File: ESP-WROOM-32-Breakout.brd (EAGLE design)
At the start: 34.5 x 40 mm, 10 parts, among them SW1 PROG, SW2 RST, U3 ESP-WROOM-32

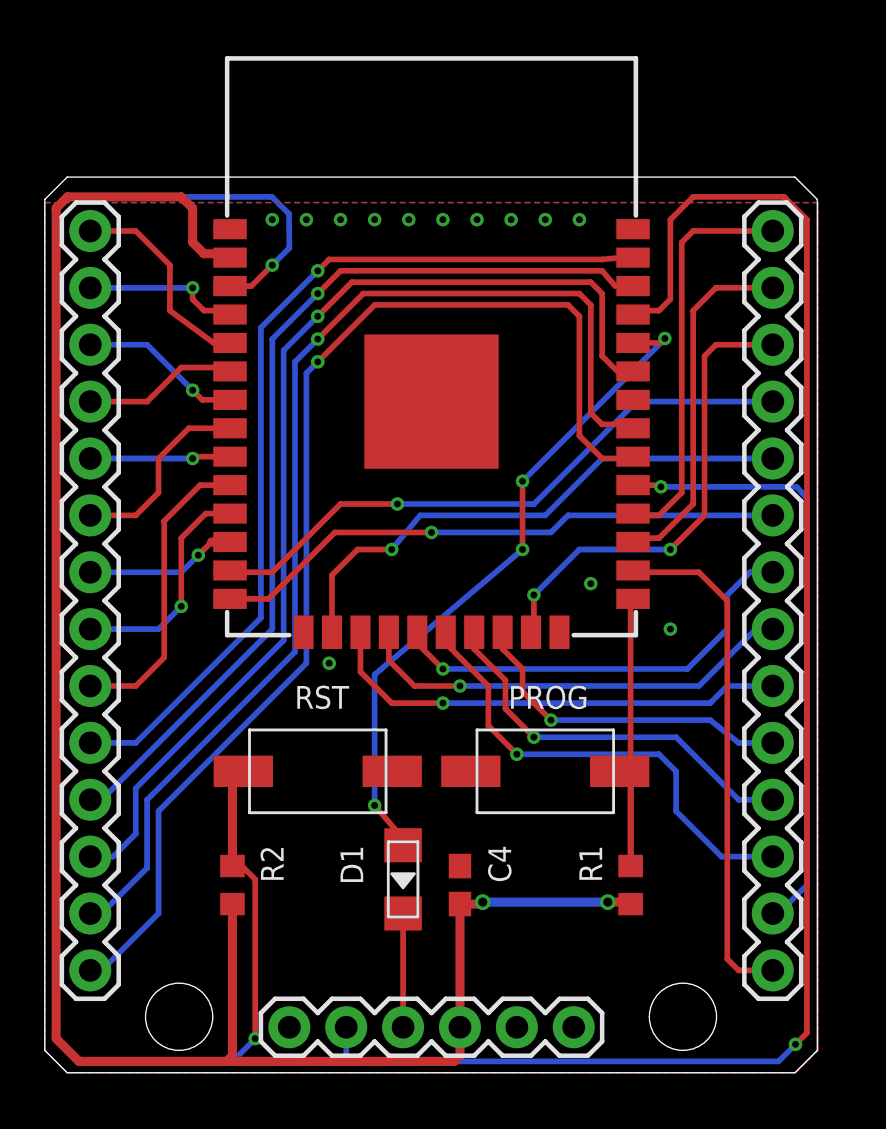
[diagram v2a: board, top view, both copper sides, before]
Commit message: added reverse-voltage protection
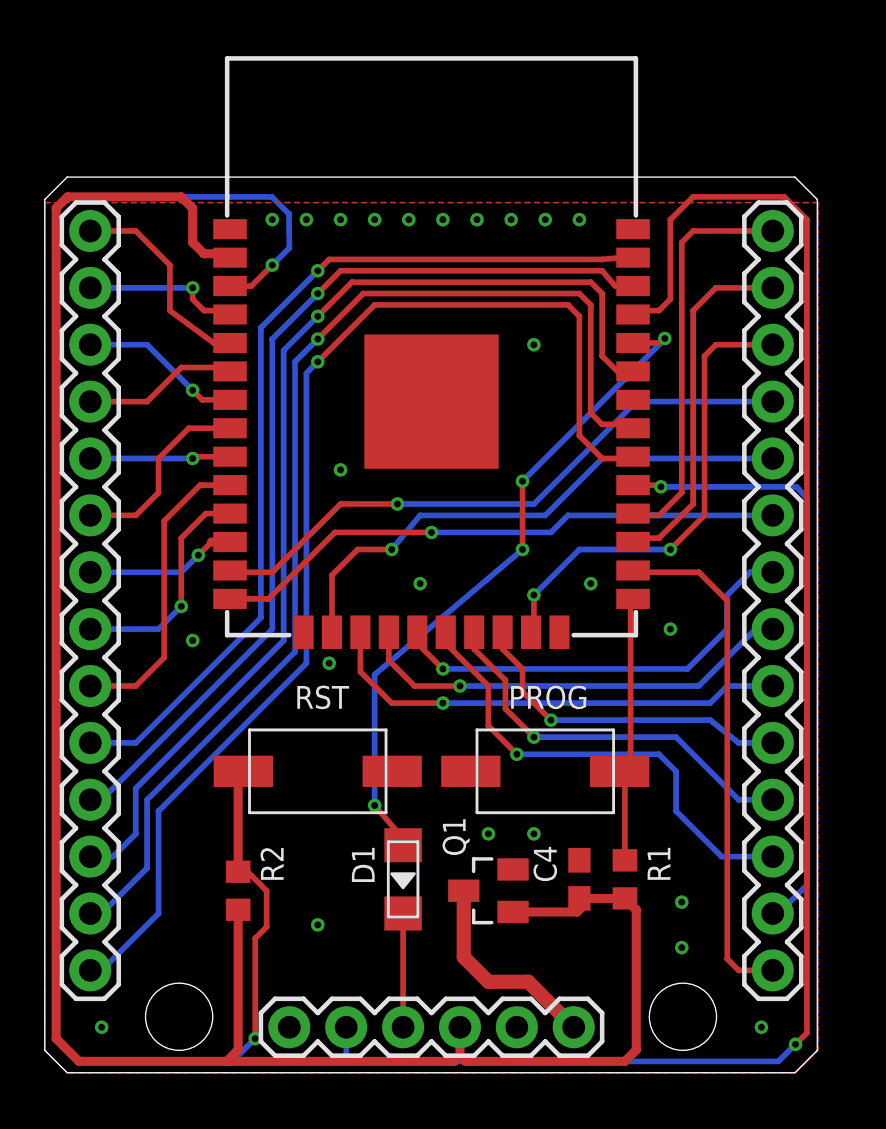
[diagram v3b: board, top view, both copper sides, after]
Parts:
- added Q1: 2N7002, nxp_60_1_1:SOT23
- moved C4 5.34 mm to (23.9, 8.64)
- moved R2 0.36 mm to (8.64, 8.13)
- moved R1 0.36 mm to (25.9, 8.64)
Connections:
- new net GND_IN: JP3.6, Q1.3
- net GND: now also Q1.2; no longer JP3.6
- net VCC: now also Q1.1
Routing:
- net GND_IN: track 0.00 -> 9.17 mm
- net VCC: track 87.2 -> 94.8 mm, vias 2 -> 0
- net IO0: track 16.4 -> 12.7 mm
- net EN: track 75.6 -> 76.4 mm
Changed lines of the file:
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@@
 </autorouter>
 <elements>
-<element name="C4" library="rcl" package="C0603" value="10u" x="18.542" y="8.382" smashed="yes" rot="R90">
-<attribute name="NAME" x="20.828" y="10.16" size="1.016" layer="25" font="vector" ratio="12" rot="R90" align="bottom-right"/>
-</element>
-<element name="R2" library="rcl" package="R0603" value="10k" x="8.382" y="8.382" smashed="yes" rot="R270">
+<element name="C4" library="rcl" package="C0603" value="10u" x="23.876" y="8.636" smashed="yes" rot="R90">
+<attribute name="NAME" x="22.86" y="10.16" size="1.016" layer="25" font="vector" ratio="12" rot="R90" align="bottom-right"/>
+</element>
+<element name="R2" library="rcl" package="R0603" value="10k" x="8.636" y="8.128" smashed="yes" rot="R270">
 <attribute name="NAME" x="9.652" y="10.16" size="1.016" layer="25" font="vector" ratio="12" rot="R270"/>
 </element>
@@
 <attribute name="VALUE" x="17.526" y="17.894" size="1.016" layer="27" font="vector" ratio="12" rot="R180" align="center"/>
 </element>
-<element name="R1" library="rcl" package="R0603" value="10k" x="26.162" y="8.382" smashed="yes" rot="R270">
-<attribute name="NAME" x="23.876" y="10.16" size="1.016" layer="25" font="vector" ratio="12" rot="R270"/>
+<element name="R1" library="rcl" package="R0603" value="10k" x="25.908" y="8.636" smashed="yes" rot="R270">
+<attribute name="NAME" x="26.924" y="10.16" size="1.016" layer="25" font="vector" ratio="12" rot="R270"/>
 </element>
 <element name="SW1" library="Seeed-OPL-Switch" package="SW2-4.0-6.0X3.0X2.5MM" value="PROG" x="22.352" y="13.462" smashed="yes">
@@
 </element>
 <element name="D1" library="Seeed-OPL-Diode" package="LL-34" value="" x="16.002" y="8.636" smashed="yes" rot="R270">
-<attribute name="NAME" x="13.208" y="10.16" size="1.016" layer="25" font="vector" ratio="12" rot="R270"/>
+<attribute name="NAME" x="13.716" y="10.16" size="1.016" layer="25" font="vector" ratio="12" rot="R270"/>
 <attribute name="VALUE" x="13.97" y="10.541" size="0.889" layer="27" font="vector" ratio="11" rot="R270"/>
 </element>
@@
 <attribute name="PROD_ID" value="CONN-08437" x="10.922" y="2.032" size="1.016" layer="27" font="vector" ratio="12" display="off"/>
 <attribute name="VALUE" x="9.652" y="-1.143" size="1.27" layer="27"/>
+</element>
+<element name="Q1" library="nxp_60_1_1" package="SOT23" value="2N7002" x="19.812" y="8.128" smashed="yes" rot="R90">
+<attribute name="NAME" x="18.796" y="9.652" size="1.016" layer="25" font="vector" ratio="12" rot="R90"/>
+<attribute name="VALUE" x="20.812" y="10.628" size="1" layer="27" font="vector" rot="R90"/>
 </element>
 </elements>
@@
 <vertex x="34.544" y="1"/>
 </polygon>
-<contactref element="JP3" pad="6"/>
 <via x="10.16" y="38.1" extent="1-16" drill="0.3048"/>
 <via x="11.684" y="38.1" extent="1-16" drill="0.3048"/>
@@
 <via x="24.384" y="21.844" extent="1-16" drill="0.3048"/>
 <via x="12.7" y="18.288" extent="1-16" drill="0.3048"/>
+<contactref element="Q1" pad="2"/>
+<via x="28.448" y="7.62" extent="1-16" drill="0.3048"/>
+<via x="28.448" y="5.588" extent="1-16" drill="0.3048"/>
+<via x="32.004" y="2.032" extent="1-16" drill="0.3048"/>
+<via x="12.192" y="6.604" extent="1-16" drill="0.3048"/>
+<via x="2.54" y="2.032" extent="1-16" drill="0.3048"/>
+<via x="6.604" y="19.304" extent="1-16" drill="0.3048"/>
+<via x="13.208" y="26.924" extent="1-16" drill="0.3048"/>
+<via x="21.844" y="32.512" extent="1-16" drill="0.3048"/>
+<via x="16.764" y="21.844" extent="1-16" drill="0.3048"/>
+<via x="19.812" y="10.668" extent="1-16" drill="0.3048"/>
+<via x="21.844" y="10.668" extent="1-16" drill="0.3048"/>
 </signal>
 <signal name="VCC" class="2">
@@
 <wire x1="7.112" y1="36.576" x2="8.098" y2="36.576" width="0.4064" layer="1"/>
 <wire x1="8.098" y1="36.576" x2="8.272" y2="36.402" width="0.4064" layer="1"/>
-<wire x1="8.382" y1="7.532" x2="8.382" y2="0.762" width="0.4064" layer="1"/>
-<wire x1="8.382" y1="0.762" x2="8.128" y2="0.508" width="0.4064" layer="1"/>
-<wire x1="18.542" y1="7.532" x2="19.47" y2="7.532" width="0.4064" layer="1"/>
-<wire x1="19.47" y1="7.532" x2="19.558" y2="7.62" width="0.4064" layer="1"/>
-<via x="19.558" y="7.62" extent="1-16" drill="0.4064"/>
-<wire x1="19.558" y1="7.62" x2="25.146" y2="7.62" width="0.4064" layer="16"/>
-<via x="25.146" y="7.62" extent="1-16" drill="0.4064"/>
-<wire x1="25.146" y1="7.62" x2="26.074" y2="7.62" width="0.4064" layer="1"/>
-<wire x1="26.074" y1="7.62" x2="26.162" y2="7.532" width="0.4064" layer="1"/>
 <contactref element="JP3" pad="4"/>
-<wire x1="18.542" y1="0.762" x2="18.542" y2="2.032" width="0.4064" layer="1"/>
-<wire x1="18.542" y1="2.032" x2="18.542" y2="7.532" width="0.4064" layer="1"/>
+<contactref element="Q1" pad="1"/>
+<wire x1="20.912" y1="7.178" x2="23.776" y2="7.178" width="0.4064" layer="1"/>
+<wire x1="23.776" y1="7.178" x2="24.047" y2="7.449" width="0.4064" layer="1"/>
+<wire x1="23.876" y1="7.62" x2="24.042" y2="7.786" width="0.4064" layer="1"/>
+<wire x1="24.042" y1="7.786" x2="25.908" y2="7.786" width="0.4064" layer="1"/>
+<wire x1="18.542" y1="2.032" x2="18.542" y2="0.762" width="0.4064" layer="1"/>
+<wire x1="18.542" y1="0.762" x2="18.796" y2="0.508" width="0.4064" layer="1"/>
+<wire x1="18.796" y1="0.508" x2="25.908" y2="0.508" width="0.4064" layer="1"/>
+<wire x1="25.908" y1="0.508" x2="26.416" y2="1.016" width="0.4064" layer="1"/>
+<wire x1="26.416" y1="1.016" x2="26.416" y2="7.278" width="0.4064" layer="1"/>
+<wire x1="26.416" y1="7.278" x2="25.908" y2="7.786" width="0.4064" layer="1"/>
+<wire x1="23.876" y1="7.786" x2="23.876" y2="7.62" width="0.4064" layer="1"/>
+<wire x1="23.876" y1="7.62" x2="24.047" y2="7.449" width="0.4064" layer="1"/>
+<wire x1="8.636" y1="7.278" x2="8.636" y2="1.016" width="0.4064" layer="1"/>
+<wire x1="8.636" y1="1.016" x2="8.128" y2="0.508" width="0.4064" layer="1"/>
 </signal>
 <signal name="EN">
@@
 <contactref element="R2" pad="1"/>
 <contactref element="SW2" pad="2"/>
-<wire x1="8.382" y1="9.232" x2="8.382" y2="12.977" width="0.4064" layer="1"/>
-<wire x1="8.382" y1="12.977" x2="8.867" y2="13.462" width="0.4064" layer="1"/>
+<wire x1="8.636" y1="8.978" x2="8.636" y2="13.208" width="0.4064" layer="1"/>
+<wire x1="8.636" y1="13.208" x2="8.867" y2="13.462" width="0.4064" layer="1"/>
 <wire x1="8.272" y1="35.132" x2="9.224" y2="35.132" width="0.254" layer="1"/>
 <wire x1="9.224" y1="35.132" x2="10.16" y2="36.068" width="0.254" layer="1"/>
@@
 <wire x1="8.382" y1="0.508" x2="9.398" y2="1.524" width="0.254" layer="16"/>
 <via x="9.398" y="1.524" extent="1-16" drill="0.3048"/>
-<wire x1="9.398" y1="1.524" x2="9.398" y2="8.636" width="0.254" layer="1"/>
-<wire x1="9.398" y1="8.636" x2="8.89" y2="9.144" width="0.254" layer="1"/>
+<wire x1="9.398" y1="1.524" x2="9.4" y2="6" width="0.254" layer="1"/>
+<wire x1="9.4" y1="6" x2="9.906" y2="6.506" width="0.254" layer="1"/>
+<wire x1="9.906" y1="6.506" x2="9.906" y2="8.128" width="0.254" layer="1"/>
+<wire x1="9.906" y1="8.128" x2="8.89" y2="9.144" width="0.254" layer="1"/>
 <wire x1="8.89" y1="9.144" x2="8.294" y2="9.144" width="0.254" layer="1"/>
-<wire x1="8.294" y1="9.144" x2="8.382" y2="9.232" width="0.4064" layer="1"/>
+<wire x1="8.294" y1="9.144" x2="8.636" y2="8.978" width="0.4064" layer="1"/>
 </signal>
 <signal name="RXD0">
@@
 <contactref element="R1" pad="1"/>
 <contactref element="SW1" pad="2"/>
-<wire x1="26.162" y1="9.232" x2="26.162" y2="12.977" width="0.254" layer="1"/>
 <wire x1="26.162" y1="12.977" x2="25.677" y2="13.462" width="0.4064" layer="1"/>
-<wire x1="26.162" y1="9.232" x2="26.162" y2="21.052" width="0.254" layer="1"/>
 <wire x1="26.162" y1="21.052" x2="26.272" y2="21.162" width="0.4064" layer="1"/>
+<wire x1="26.162" y1="21.052" x2="26.162" y2="14.052209375" width="0.254" layer="1"/>
+<wire x1="26.162" y1="14.052209375" x2="26.08760625" y2="13.87260625" width="0.254" layer="1" curve="-44.999502"/>
+<wire x1="26.08760625" y1="13.87260625" x2="25.677" y2="13.462" width="0.254" layer="1"/>
+<wire x1="25.908" y1="9.486" x2="25.908" y2="13.125790625" width="0.254" layer="1"/>
+<wire x1="25.908" y1="13.125790625" x2="25.83360625" y2="13.30539375" width="0.254" layer="1" curve="44.999502"/>
+<wire x1="25.83360625" y1="13.30539375" x2="25.677" y2="13.462" width="0.254" layer="1"/>
 </signal>
 <signal name="TXD0">
@@
 <wire x1="2.032" y1="37.592" x2="4.064" y2="37.592" width="0.254" layer="1"/>
 </signal>
+<signal name="GND_IN" class="1">
+<contactref element="JP3" pad="6"/>
+<contactref element="Q1" pad="3"/>
+<wire x1="18.712" y1="8.128" x2="18.712" y2="5.164" width="0.635" layer="1"/>
+<wire x1="18.712" y1="5.164" x2="19.812" y2="4.064" width="0.635" layer="1"/>
+<wire x1="19.812" y1="4.064" x2="21.59" y2="4.064" width="0.635" layer="1"/>
+<wire x1="21.59" y1="4.064" x2="23.622" y2="2.032" width="0.635" layer="1"/>
+</signal>
 </signals>

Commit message: changed diode package to SOD-323
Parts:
- D1: device Seeed-OPL-Diode:LL-34 -> Seeed-OPL-Diode:SOD-323
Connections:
- net RX: now also D1.-; no longer D1.C
- net RXD0: now also D1.+; no longer D1.A
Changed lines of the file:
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@@
 <attribute name="VALUE" x="13.589" y="17.272" size="1.016" layer="25" font="vector" ratio="12" rot="R180"/>
 </element>
-<element name="D1" library="Seeed-OPL-Diode" package="LL-34" value="" x="16.002" y="8.636" smashed="yes" rot="R270">
+<element name="D1" library="Seeed-OPL-Diode" package="SOD-323" value="" x="16.002" y="8.636" smashed="yes" rot="R270">
 <attribute name="NAME" x="13.716" y="10.16" size="1.016" layer="25" font="vector" ratio="12" rot="R270"/>
 <attribute name="VALUE" x="13.97" y="10.541" size="0.889" layer="27" font="vector" ratio="11" rot="R270"/>
@@
 <signal name="RXD0">
 <contactref element="U3" pad="34"/>
-<contactref element="D1" pad="A"/>
+<contactref element="D1" pad="+"/>
 <wire x1="26.272" y1="32.592" x2="27.492" y2="32.592" width="0.254" layer="1"/>
 <wire x1="27.492" y1="32.592" x2="27.692" y2="32.792" width="0.254" layer="1"/>
@@
 <via x="14.732" y="11.938" extent="1-16" drill="0.3048"/>
 <wire x1="14.732" y1="11.938" x2="16.256" y2="10.16" width="0.254" layer="1"/>
-<wire x1="16.256" y1="10.16" x2="16.002" y2="10.16" width="0.254" layer="1"/>
+<wire x1="16.256" y1="10.16" x2="16.002" y2="9.836" width="0.254" layer="1"/>
 </signal>
 <signal name="IO0">
@@
 </signal>
 <signal name="RX">
-<contactref element="D1" pad="C"/>
+<contactref element="D1" pad="-"/>
 <contactref element="JP3" pad="3"/>
-<wire x1="16.002" y1="2.032" x2="16.002" y2="7.112" width="0.254" layer="1"/>
+<wire x1="16.002" y1="2.032" x2="16.002" y2="7.436" width="0.254" layer="1"/>
 </signal>
 <signal name="IO34">
